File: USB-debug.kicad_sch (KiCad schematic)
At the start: 39 parts, among them J4 USB-C_GCT_USB4145-03-0070-C, Q25 BSS138PW, Q4 BSS138PW, U16 TPD4E05U06QDQARQ1, U31 FT4232H_VQFN, Y3 Oscillator_12MHz_ASFLMB

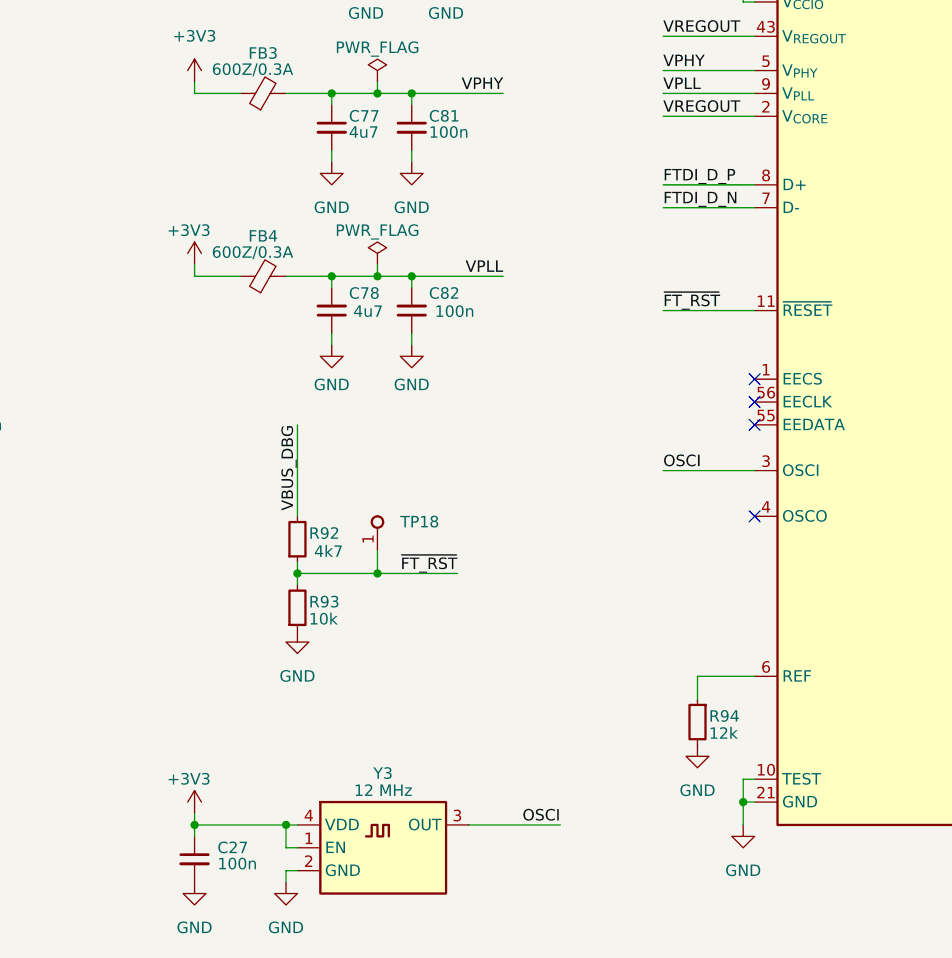
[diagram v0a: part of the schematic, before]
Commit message: [#72133] Unify 12MHz generators
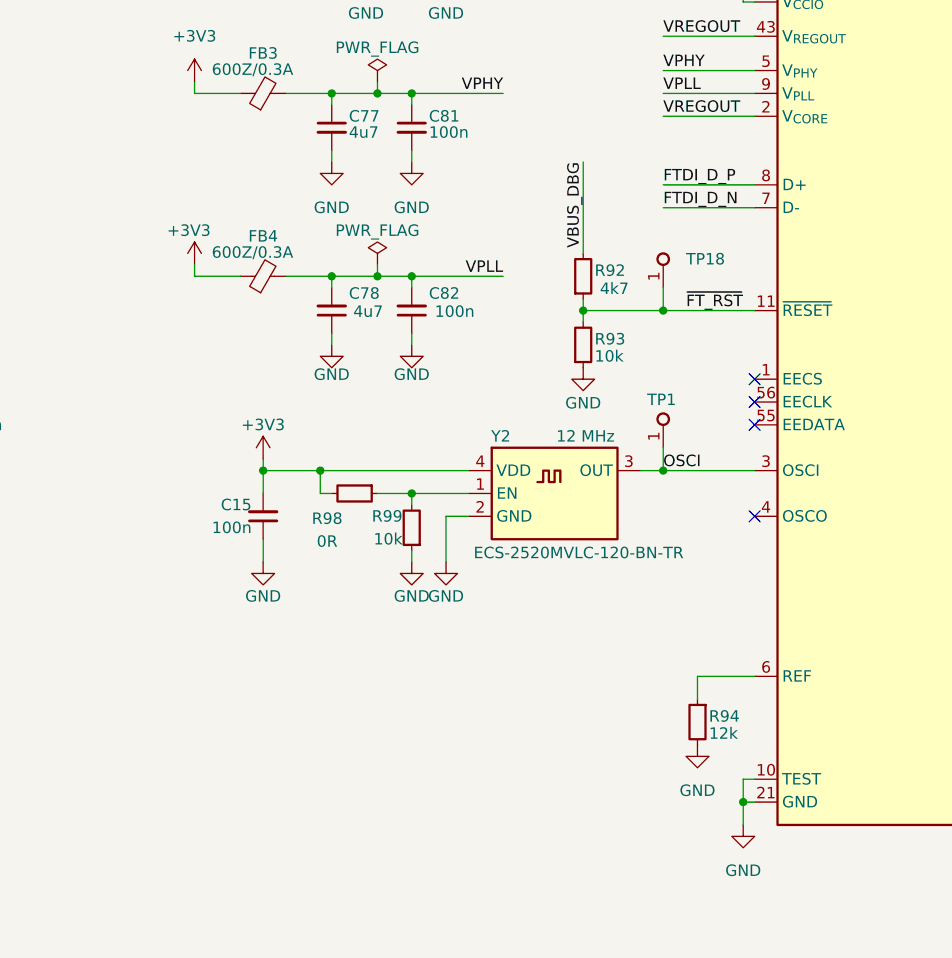
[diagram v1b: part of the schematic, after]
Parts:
- removed C27: C_100n_16V_X7R_0402, antmicro-footprints:C_0402_1005Metric, symbol antmicroCapacitors0402:C_100n_16V_X7R_0402
- removed Y3: Oscillator_12MHz_ASFLMB, antmicro-footprints:Oscillator_SMD_Abracon_ASFLMB_5x3.2x0.85mm, symbol antmicroOscillators:Oscillator_12MHz_ASFLMB
- added C15: C_100n_0402, antmicro-footprints:C_0402_1005Metric, symbol antmicroCapacitors0402:C_100n_0402
- added R98: R_0R_0402, antmicro-footprints:R_0402_1005Metric, symbol antmicroResistors0402:R_0R_0402
- added R99: R_10k_0402, antmicro-footprints:R_0402_1005Metric, symbol antmicroResistors0402:R_10k_0402
- added TP1: TP_0.75mm_SMD, antmicro-footprints:TP_SMD_0.75mm, symbol antmicroTestPoints:TP_0.75mm_SMD
- added Y2: Oscillator_12MHz_ESC_2520MV, antmicro-footprints:Oscillator_SMD_ECS_2520MV_2.5x2mm, symbol antmicroOscillators:Oscillator_12MHz_ESC_2520MV
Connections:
- net +3V3: now also C15.2, R98.2, Y2.4 (VDD)
- net GND: now also C15.1, R99.1, Y2.2 (GND)
- net OSCI: now also TP1.1, Y2.3 (OUT)
- new net: R98.1, R99.2, Y2.1 (EN)
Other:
- moved on the sheet: R92, R93, TP18

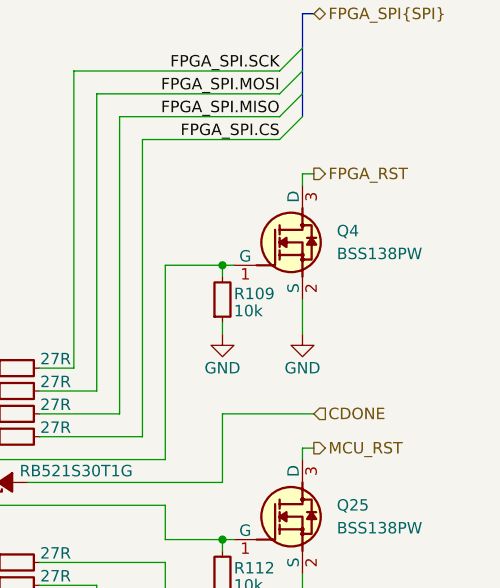
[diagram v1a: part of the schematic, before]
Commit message: [#72133] Clean ERC
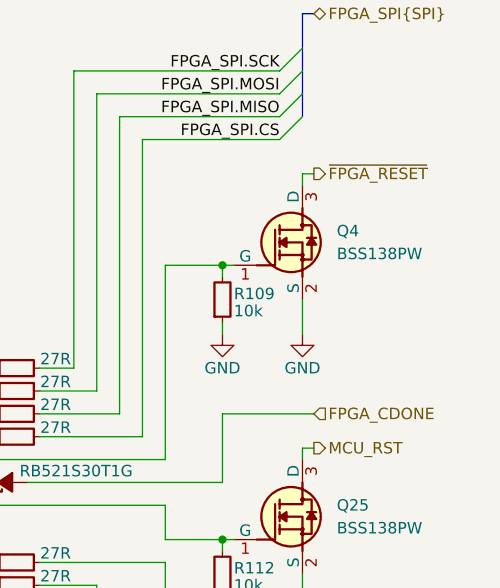
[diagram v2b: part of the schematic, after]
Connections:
- net CDONE renamed FPGA_CDONE
- net FPGA_RST renamed ~{FPGA_RESET}
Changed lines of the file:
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@@
 		)
 	)
-	(hierarchical_label "CDONE"
+	(hierarchical_label "FPGA_CDONE"
 		(shape input)
 		(at 255.27 63.5 0)
@@
 		)
 	)
-	(hierarchical_label "FPGA_RST"
+	(hierarchical_label "~{FPGA_RESET}"
 		(shape output)
 		(at 255.27 36.83 0)
@@
 			)
 		)
-		(property "Datasheet" "https://www.ftdichip.com/Support/Documents/DataSheets/ICs/DS_FT4232H.pdf"
+		(property "Datasheet" "https://ftdichip.com/wp-content/uploads/2024/09/DS_FT4232H.pdf"
 			(at 219.71 68.58 0)
 			(effects
@@
 			)
 		)
-		(property "Description" ""
+		(property "Description" "Interface Bridges, USB to UART, MPSSE, 1.62 V, 1.98 V, VQFN, 56 Pins, -40 °C"
 			(at 163.83 58.42 0)
 			(effects

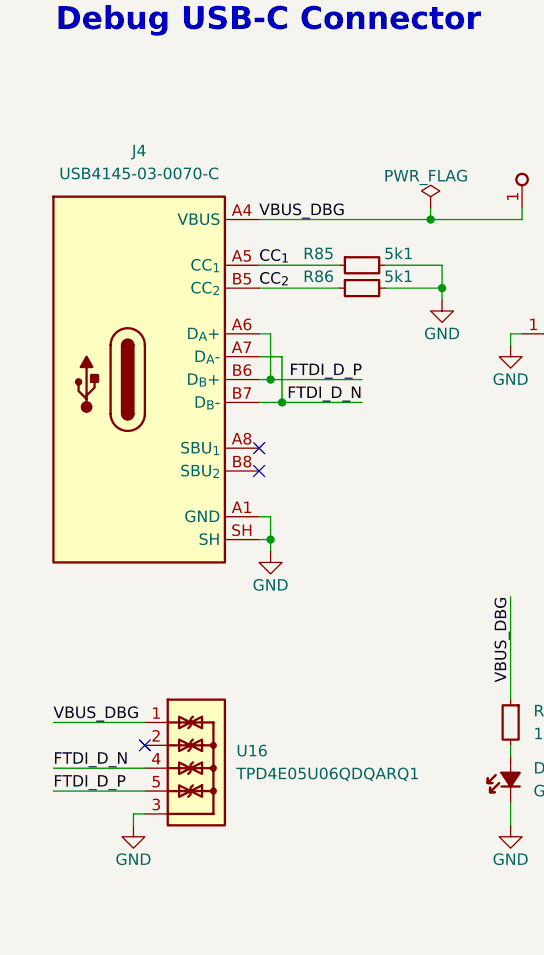
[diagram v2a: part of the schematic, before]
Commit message: [#72447] Change connectors to horizontal
Signed-off-by: Dawid Lentka <dlentka@antmicro.com>
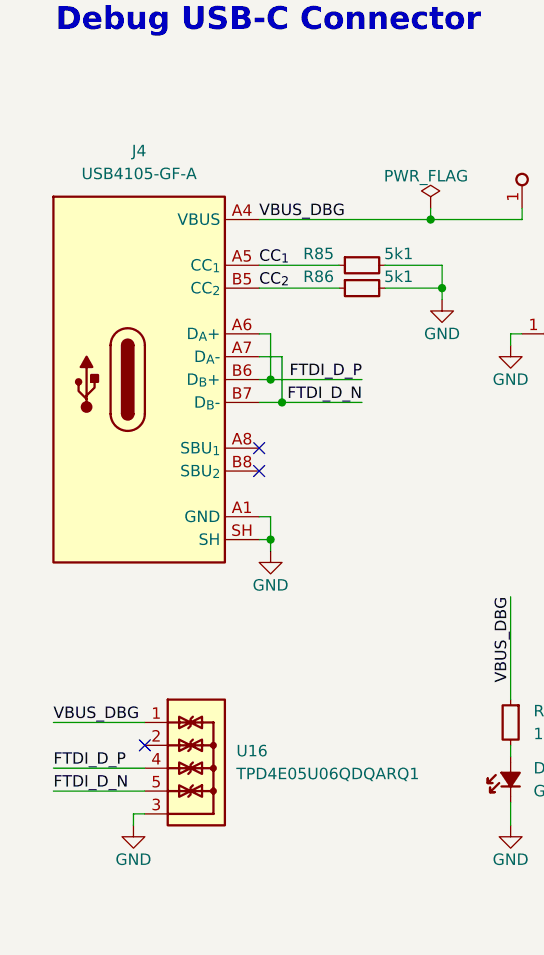
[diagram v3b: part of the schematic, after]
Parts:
- J4: value USB-C_GCT_USB4145-03-0070-C -> USB-C_GCT_USB4105-GF-A; footprint antmicro-footprints:USB-C_Receptacle_GCT_USB4145-03-0070-C -> antmicro-footprints:USB-C_Receptacle_GCT_USB4105-GF-A; symbol antmicroUSBConnectors:USB-C_GCT_USB4145-03-0070-C -> antmicroUSBConnectors:USB-C_GCT_USB4105-GF-A; MPN USB4145-03-0070-C -> USB4105-GF-A
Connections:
- net FTDI_D_N: now also U16.5, U16.6; no longer U16.4, U16.7
- net FTDI_D_P: now also U16.4, U16.7; no longer U16.5, U16.6
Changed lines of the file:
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@@
 	)
 	(label "FTDI_D_P"
-		(at 21.59 107.95 0)
+		(at 21.59 105.41 0)
 		(fields_autoplaced yes)
 		(effects
@@
 	)
 	(label "FTDI_D_N"
-		(at 21.59 105.41 0)
+		(at 21.59 107.95 0)
 		(fields_autoplaced yes)
 		(effects
@@
 	)
 	(symbol
-		(lib_id "antmicroUSBConnectors:USB-C_GCT_USB4145-03-0070-C")
+		(lib_id "antmicroUSBConnectors:USB-C_GCT_USB4105-GF-A")
 		(at 44.45 44.45 0)
 		(unit 1)
@@
 			)
 		)
-		(property "Value" "USB-C_GCT_USB4145-03-0070-C"
+		(property "Value" "USB-C_GCT_USB4105-GF-A"
 			(at 31.115 39.37 0)
 			(effects
@@
 			)
 		)
-		(property "Footprint" "antmicro-footprints:USB-C_Receptacle_GCT_USB4145-03-0070-C"
+		(property "Footprint" "antmicro-footprints:USB-C_Receptacle_GCT_USB4105-GF-A"
 			(at 66.04 54.61 0)
 			(effects
@@
 			)
 		)
-		(property "Datasheet" "https://gct.co/files/drawings/usb4145.pdf"
+		(property "Datasheet" "https://gct.co/files/drawings/usb4105.pdf"
 			(at 66.04 57.15 0)
 			(effects
@@
 			)
 		)
-		(property "Description" "USB-C (USB TYPE-C) USB 2.0 Receptacle Connector 24 (16+8 Dummy) Postion  Surface Mount, Vertical"
+		(property "Description" "USB-C (USB TYPE-C) USB 2.0 Receptacle Connector 24 (16+8 Dummy) Position Surface Mount, Right Angle"
 			(at 44.45 44.45 0)
 			(effects
@@
 			)
 		)
-		(property "MPN" "USB4145-03-0070-C"
+		(property "MPN" "USB4105-GF-A"
 			(at 31.115 39.37 0)
 			(effects

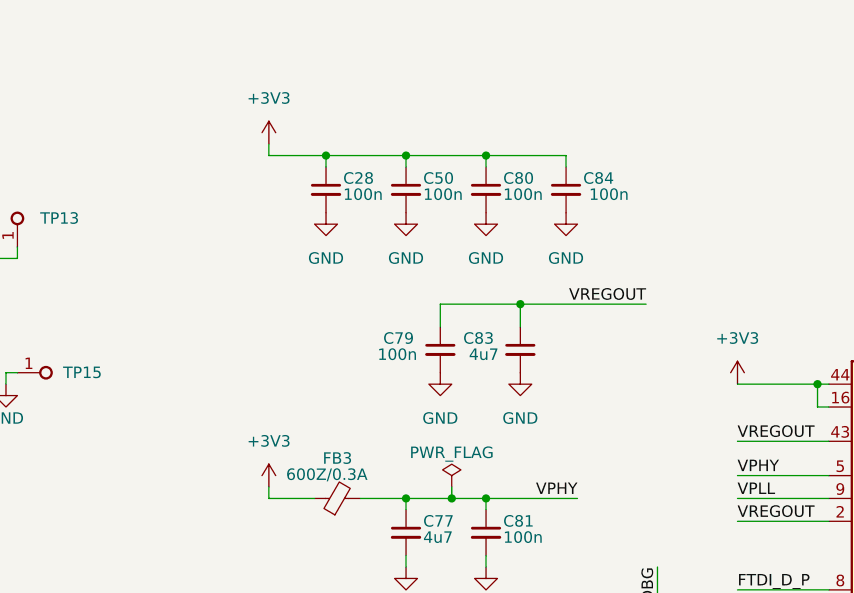
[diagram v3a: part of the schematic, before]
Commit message: [#72447] Add more capcitors to FTDI
Signed-off-by: Dawid Lentka <dlentka@antmicro.com>
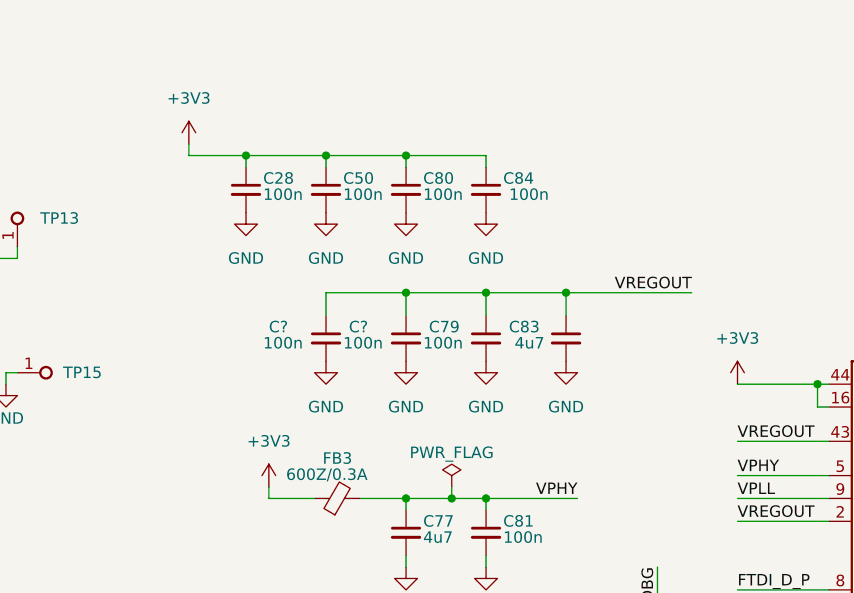
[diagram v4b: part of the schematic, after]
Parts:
- added C? (x2): C_100n_16V_X7R_0402, antmicro-footprints:C_0402_1005Metric, symbol antmicroCapacitors0402:C_100n_16V_X7R_0402
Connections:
- net GND: now also C?.2, C?.2
- net VREGOUT: now also C?.1, C?.1
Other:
- moved on the sheet: C28, C50, C79, C80, C83, C84

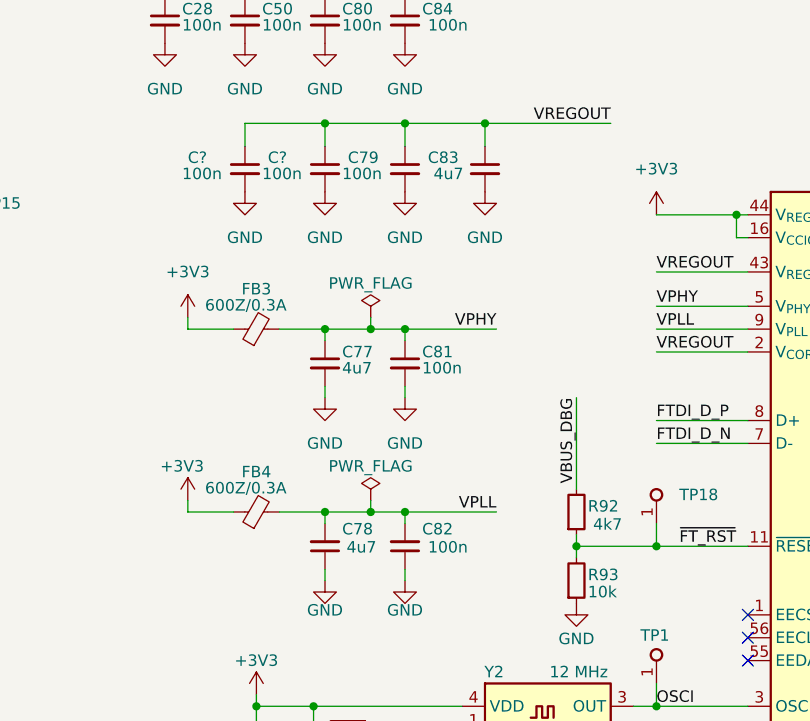
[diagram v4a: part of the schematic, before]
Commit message: [#72447] Unify capacitors
Signed-off-by: Dawid Lentka <dlentka@antmicro.com>
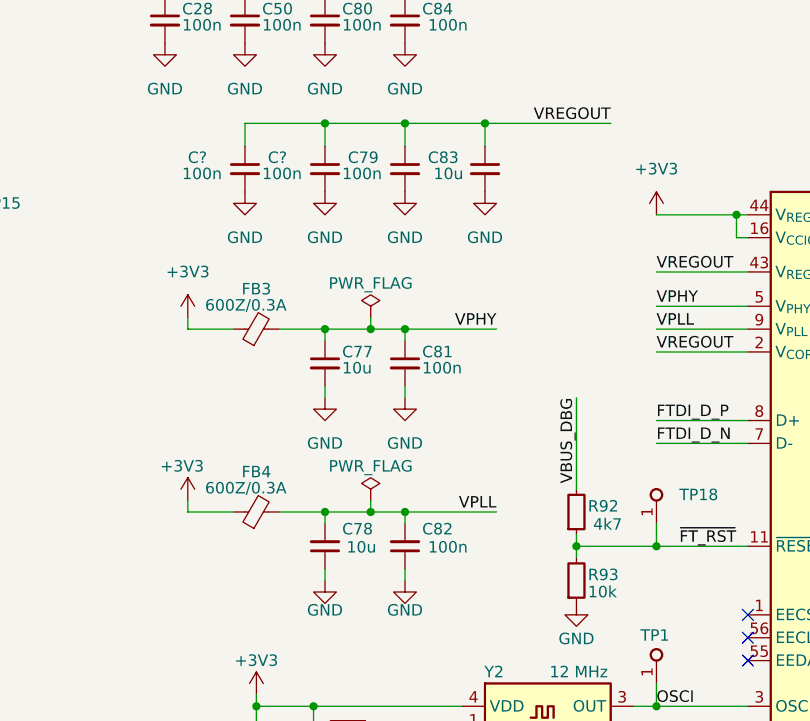
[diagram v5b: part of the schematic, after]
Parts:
- C28, C50, C79, C80, C81, C82, C84, C? (x2): value C_100n_16V_X7R_0402 -> C_100n_0402; symbol antmicroCapacitors0402:C_100n_16V_X7R_0402 -> antmicroCapacitors0402:C_100n_0402; Dielectric X7R -> X5R; MPN C0402C104J4RAC7411 -> GRM155R61H104KE14D; Manufacturer KEMET -> Murata; Voltage 16V -> 50V
- C77, C78, C83: value C_4u7_0402 -> C_10u_0402; symbol antmicroCapacitors0402:C_4u7_0402 -> antmicroCapacitors0402:C_10u_0402; MPN GRM155R61A475MEAAD -> CC0402MRX5R5BB106; Manufacturer Murata -> YAGEO; Val 4u7 -> 10u

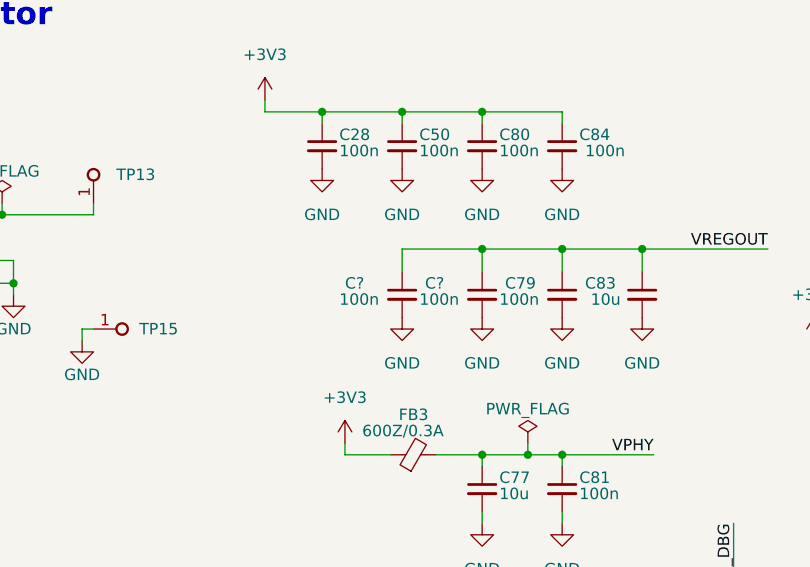
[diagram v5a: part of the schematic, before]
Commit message: [#72447] Update clock & SPI connections
Signed-off-by: Dawid Lentka <dlentka@antmicro.com>
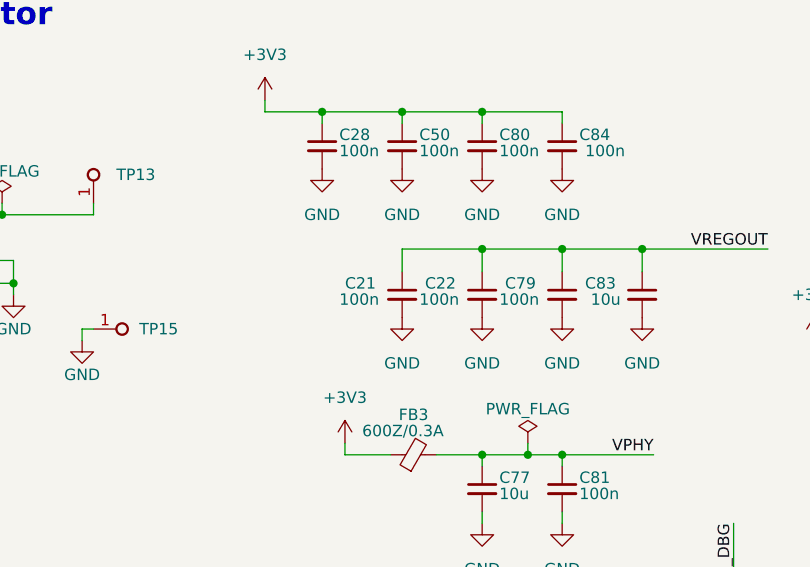
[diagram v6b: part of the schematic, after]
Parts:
- gave numbers to parts that had none: 2
